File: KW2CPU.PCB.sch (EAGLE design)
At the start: 50 parts, among them IC1 AT45DB161D8S1

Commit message: Working on layout
...4 layers is kind of annoying.
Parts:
- added IC2: (no value), microchip:MCP1804T-3302I
- added R$1: (no value), GW-devices:RF-C
- added U$10, U$11, U$8, U$9: (no value), GW-devices:RF-R0402
- C$10: MFGN (none) -> TDK; MFGP (none) -> C0603C0G1E5R1C030BG
- C$13, C$15, C$16: NOTES (none) -> DNP
- C$18: NOTE (none) -> DNP
- C$20, C$21, C$22, C$24: MFGN (none) -> Murata; MFGP (none) -> GJM1555C1H8R0CB01D
- C$6: MFGN (none) -> TDK; MFGP (none) -> C0603C0G1E1R2B030BF
- C$9: MFGN (none) -> TDK; MFGP (none) -> C0603X5R0J105M030BC
- L$11: MFGN (none) -> Murata; MFGP (none) -> BLM15AG100SN1D
- L$4, L$5: MFGN (none) -> Murata; MFGP (none) -> LQP03TN1N0B02
- R$19, R$23: MFGN (none) -> Panasonic; MFGP (none) -> ERJ-2GEJ513X
- R$7, R$8: MFGN (none) -> Panasonic; MFGP (none) -> ERJ-1GN0R00C
- U$3: MFGN (none) -> RFMD; MFGP (none) -> RF6555
- U$5: MFGN (none) -> Molex; MFGP (none) -> 0734152061
- renumbered L$6 to C$6, R$4 to L$4, R$5 to L$5
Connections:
- new net N$29: R$1.1, U$3.C_LNA
- new net N$51: IC1.!CS, U$8.1
- new net N$52: IC1.SCK, U$9.1
- new net N$53: IC1.SI, U$10.1
- new net N$54: IC1.SO, U$11.1
- new net VIN: IC2.IN, U$6.P$38, U$6.P$40
- net +3V3: now also IC2.OUT, U$6.P$37, U$6.P$39
- net GND: now also IC2.GND, IC2.P$1, R$1.2, U$6.P$1, U$6.P$2, U$6.P$3, U$6.P$4; no longer U$3.C_LNA
- net N$10: now also U$6.P$8; no longer U$6.P$4
- net N$11: now also U$6.P$10; no longer U$6.P$6
- net N$12: now also U$6.P$12; no longer U$6.P$8
- net N$13: now also U$6.P$14; no longer U$6.P$10
- net N$14: now also U$6.P$6; no longer U$6.P$2
- net N$15: now also U$6.P$16; no longer U$6.P$12
- net N$16: now also U$6.P$24, U$9.2; no longer IC1.SCK
- net N$17: now also U$10.2, U$6.P$26; no longer IC1.SI
- net N$18: now also U$11.2, U$6.P$28; no longer IC1.SO
- net N$33: now also U$6.P$7; no longer U$6.P$3
- net N$34: now also U$6.P$5; no longer U$6.P$1
- net N$35: now also U$6.P$9; no longer U$6.P$5
- net N$36: now also U$6.P$11; no longer U$6.P$7
- net N$37: now also U$6.P$13; no longer U$6.P$9
- net N$38: now also U$6.P$15; no longer U$6.P$11
- net N$39: now also U$6.P$17; no longer U$6.P$13
- net N$40: now also U$6.P$19; no longer U$6.P$15
- net N$41: now also U$6.P$21; no longer U$6.P$17
- net N$42: now also U$6.P$23; no longer U$6.P$19
- net N$43: now also U$6.P$25; no longer U$6.P$21
- net N$44: now also U$6.P$27; no longer U$6.P$23
- net N$45: now also U$6.P$29; no longer U$6.P$25
- net N$46: now also U$6.P$31; no longer U$6.P$27
- net N$47: now also U$6.P$33; no longer U$6.P$29
- net N$48: now also U$6.P$35; no longer U$6.P$31
- net N$49: now also U$6.P$18; no longer U$6.P$14
- net N$50: now also U$6.P$20; no longer U$6.P$16
- net N$7: now also U$6.P$22, U$8.2; no longer IC1.!CS
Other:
- moved on the sheet: IC1, R2, R3

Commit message: Added JTAG
Topside connector. Still needs routing
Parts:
- added U$12: MOLEX55560-0207, KW2:MOLEX55560-0207
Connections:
- net +3V3: now also U$12.P$2
- net GND: now also U$12.P$10, U$12.P$16, U$12.P$18, U$12.P$20, U$12.P$4, U$12.P$6
- net N$10: now also U$12.P$3
- net N$11: now also U$12.P$7
- net N$12: now also U$12.P$5
- net N$13: now also U$12.P$1
- net N$14: now also U$12.P$9
- net N$40: now also U$12.P$11
- net N$41: now also U$12.P$19
- net N$42: now also U$12.P$17
- net N$43: now also U$12.P$15
- net N$44: now also U$12.P$13

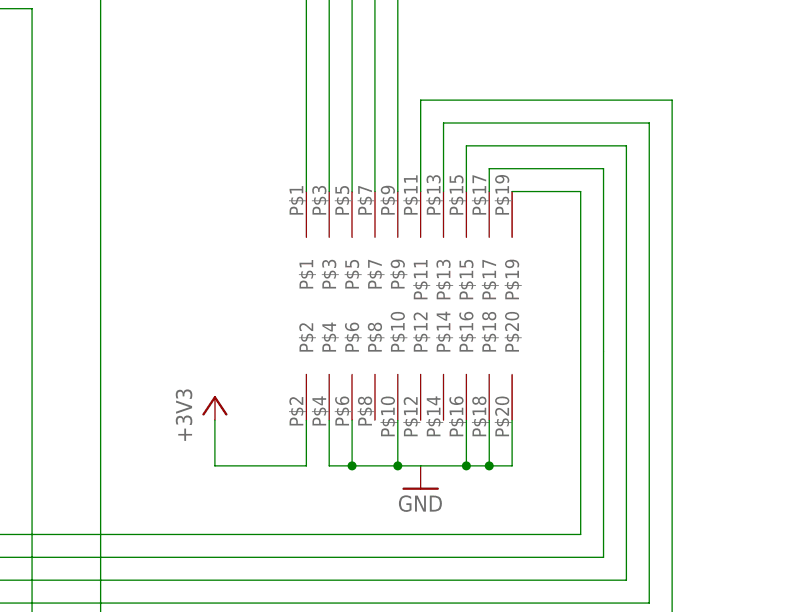
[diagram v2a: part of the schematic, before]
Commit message: JTAG, RF Conn trace
Added JTAG connector, adjusted arcs on RF connector trace and added GND
vias
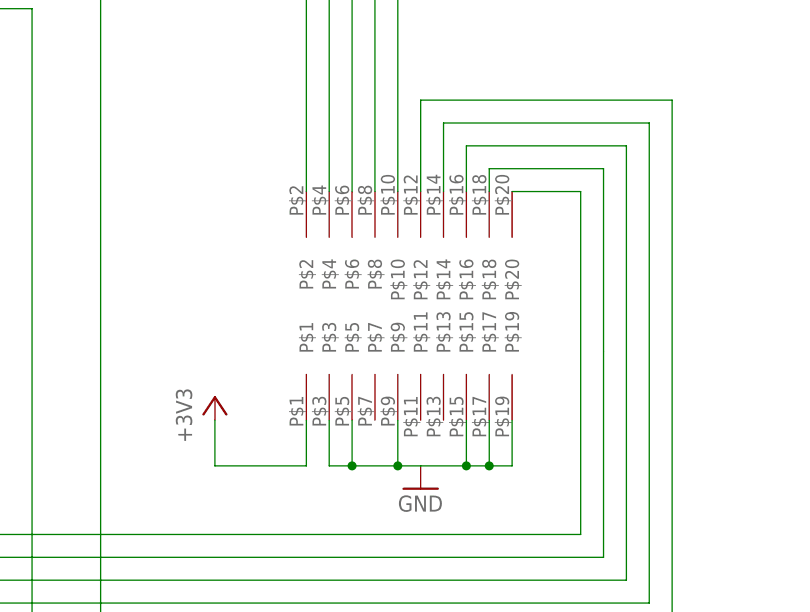
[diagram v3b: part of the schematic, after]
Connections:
- net +3V3: now also U$12.P$1; no longer U$12.P$2
- net GND: now also U$12.P$15, U$12.P$17, U$12.P$19, U$12.P$3, U$12.P$5, U$12.P$9; no longer U$12.P$10, U$12.P$16, U$12.P$18, U$12.P$20, U$12.P$4, U$12.P$6
- net N$10: now also U$12.P$4; no longer U$12.P$3
- net N$11: now also U$12.P$8; no longer U$12.P$7
- net N$12: now also U$12.P$6; no longer U$12.P$5
- net N$13: now also U$12.P$2; no longer U$12.P$1
- net N$14: now also U$12.P$10; no longer U$12.P$9
- net N$40: now also U$12.P$12; no longer U$12.P$11
- net N$41: now also U$12.P$20; no longer U$12.P$19
- net N$42: now also U$12.P$18; no longer U$12.P$17
- net N$43: now also U$12.P$16; no longer U$12.P$15
- net N$44: now also U$12.P$14; no longer U$12.P$13

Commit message: Rotated board
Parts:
- added LED1: (no value), adafruit:LEDCHIPLED_0805
- added SJ1: (no value), jumper:SJ
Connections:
- net GND: now also R$23.2
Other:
- moved on the sheet: C$10, C$13, C$15, C$16, C$18, C$20, C$21, C$22, C$24, C$6, C$9, IC2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

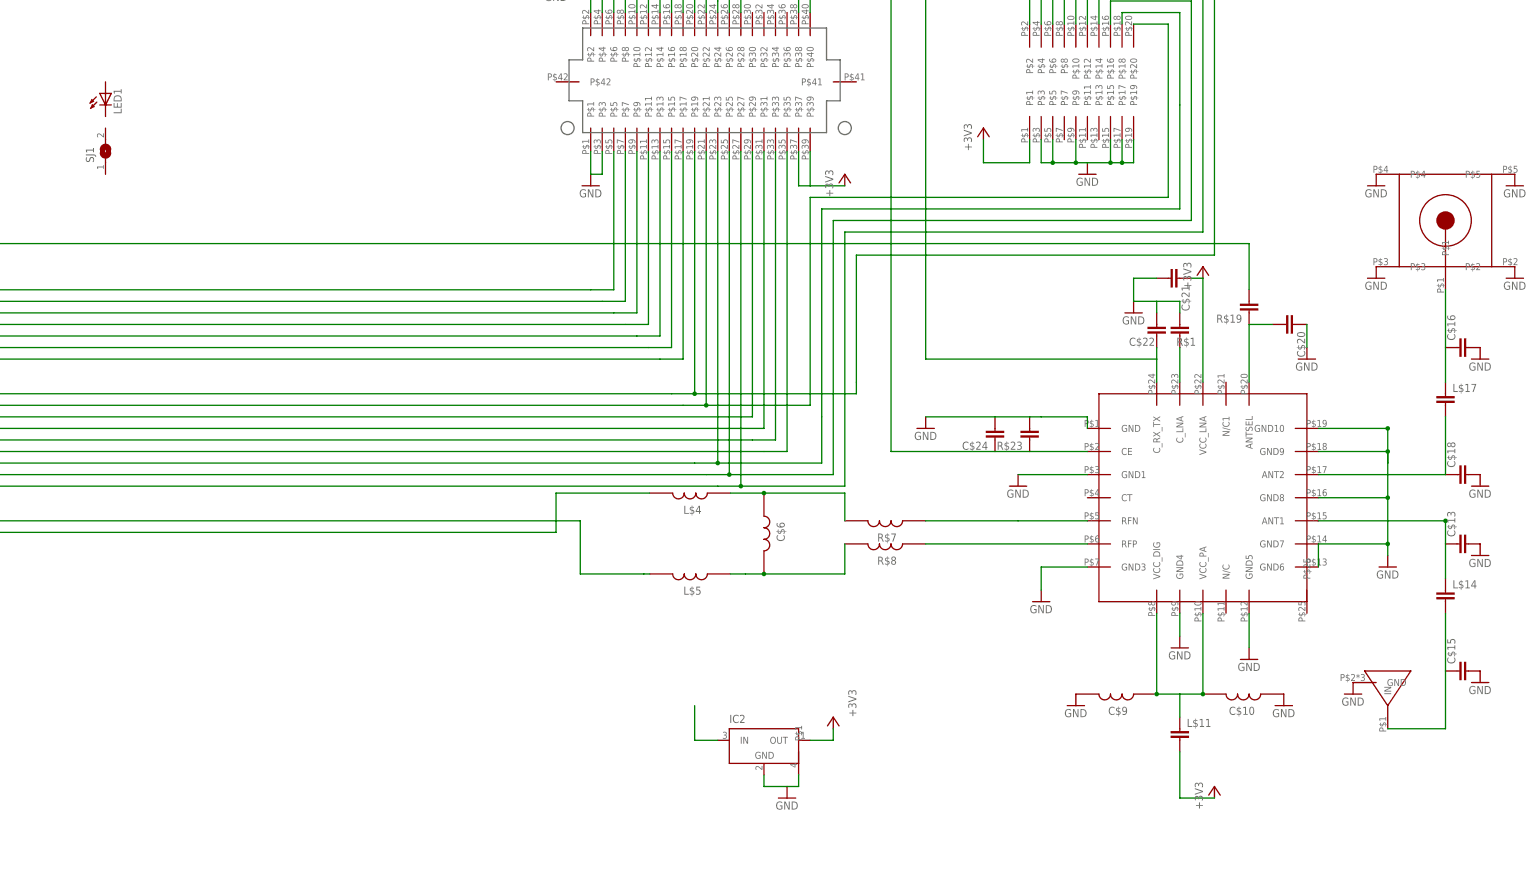
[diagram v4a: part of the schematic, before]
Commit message: Schematic fix
Almost done fixing schematic
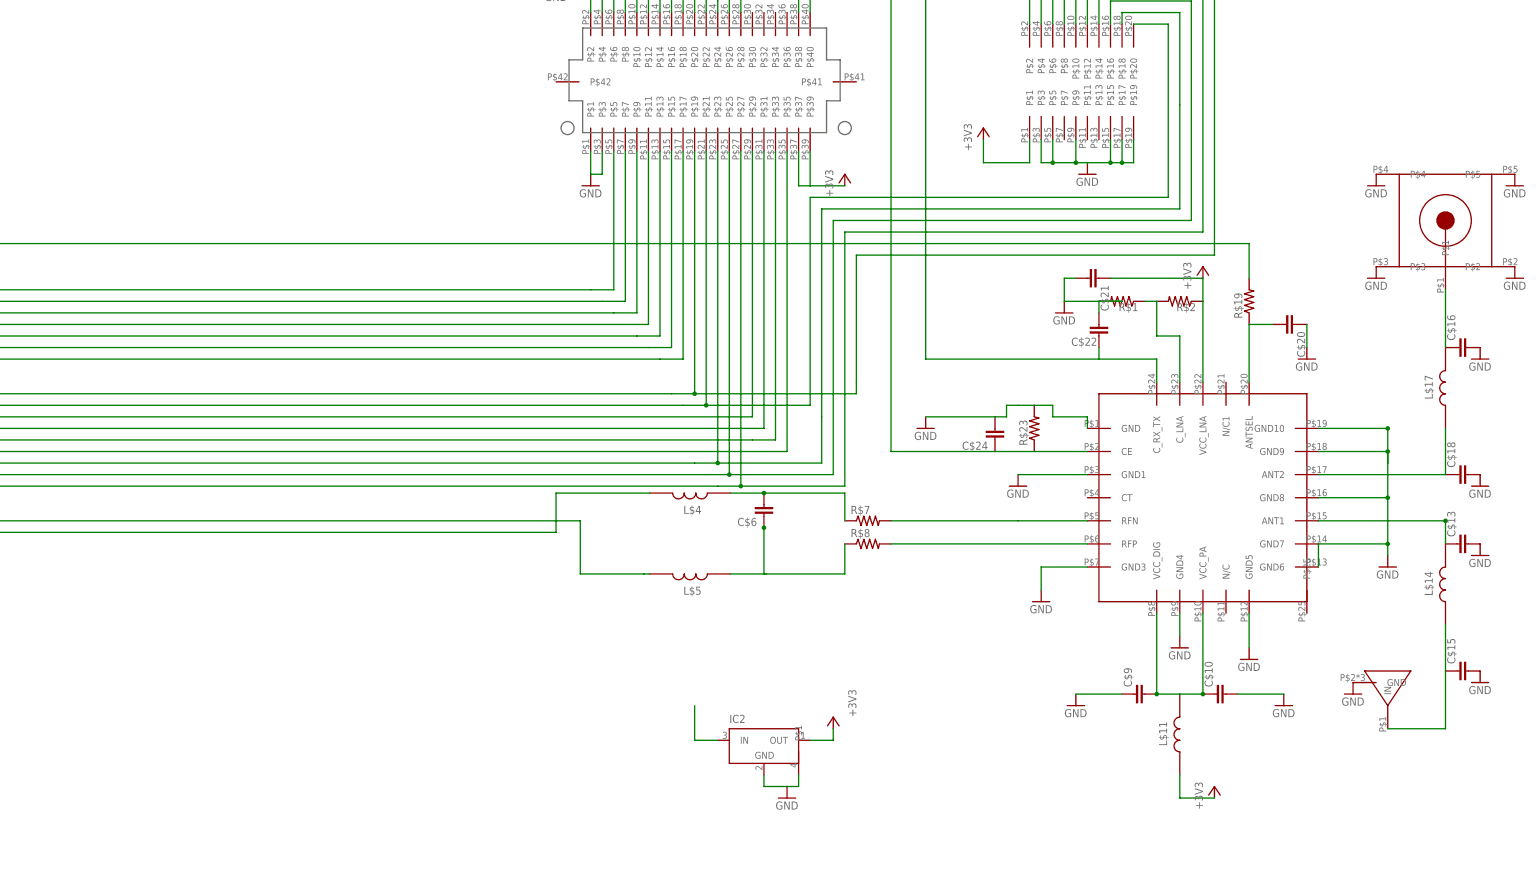
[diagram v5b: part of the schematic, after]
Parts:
- removed LED1: (no value), adafruit:LEDCHIPLED_0805
- removed SJ1: (no value), jumper:SJ
- added R$2: (no value), GW-devices:RF-RRFMD
- C$10, C$6, C$9: device GW-devices:RF-L -> GW-devices:RF-C
- C$13, C$15, C$16, C$18, C$20, C$21, C$22, C$24: device GW-devices:RF-C -> GW-devices:RF-CRFMD
- L$11, L$14, L$17: device GW-devices:RF-C -> GW-devices:RF-L
- L$4, L$5: device GW-devices:RF-L -> GW-devices:RF-L0201
- R$1, R$19, R$23: device GW-devices:RF-C -> GW-devices:RF-RRFMD
- R$7, R$8: device GW-devices:RF-L -> GW-devices:RF-R
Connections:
- net +3V3: now also R$2.1
- net N$29: now also R$2.2
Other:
- moved on the sheet: C$21, C$22
